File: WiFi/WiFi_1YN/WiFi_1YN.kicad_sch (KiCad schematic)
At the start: 9 parts, among them J1 ANT, J2 DF40C-20DP-0.4V_51_, J3 DF40C-20DP-0.4V_51_, U1 LBEE5KL1YN-814, Y1 ECS-327MVATX-3-CN-TR3

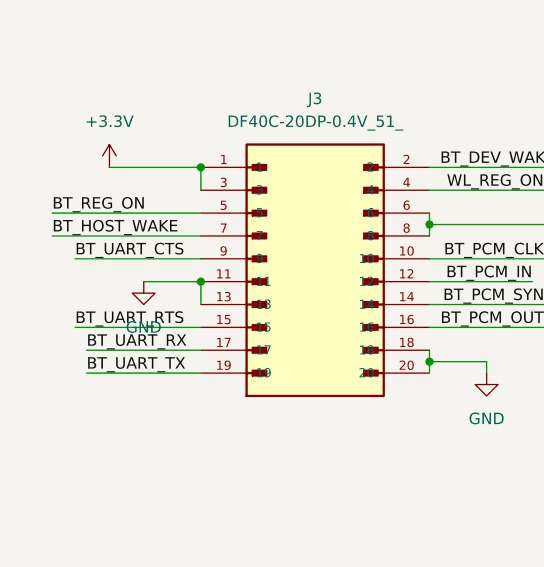
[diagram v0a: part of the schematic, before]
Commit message: fix the rts/cts line being swapped and missing led0 connection (PWM0)
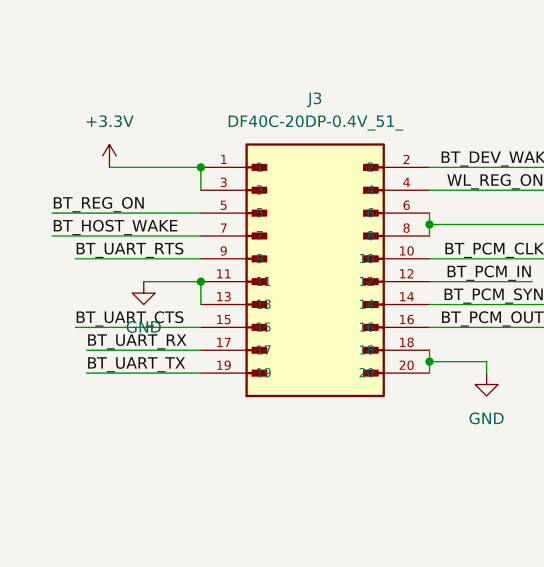
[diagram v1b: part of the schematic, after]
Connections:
- net BT_UART_CTS: now also J3.15; no longer J3.9
- net BT_UART_RTS: now also J3.9; no longer J3.15
